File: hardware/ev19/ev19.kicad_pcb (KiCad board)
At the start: 4 copper layers, 173.8 x 91 mm, 254 parts, among them CN1 Conn_05x02_Female, CN3 BM14B(0.8)-24DS-0.4V(53), J1 USB_C_Receptacle, J10 USB_C_Receptacle, J11 Conn_02x05_Counter_Clockwise, J12 PJ-242, J2 Conn_01x02_Socket, J3 AudioJack4, J4 Conn_02x03_Odd_Even, J5 Conn_02x03_Odd_Even, J6 Conn_02x05_Counter_Clockwise, J7 Conn_02x05_Counter_Clockwise, J8 Conn_02x05_Counter_Clockwise, J9 Conn_02x05_Counter_Clockwise, Q1 2N7002, Q2 2N7002, Q3 2N7002, Q4 2N7002, Q5 2N7002, Q6 2N7002, SW1 SW_SPDT, SW2 SW_Push, SW3 SW_Push, SW4 SW_Push, SW5 SW_Push, SW6 SW_Push, SW7 SW_Push, U1 BQ21040DBV, U10 STM32F405RGTx, U12 XC6227C301MR-G, U2 USBLC6-2P6, U3 STM32F072CBTx, U4 CH340C, U5 TPS63060, U6 ES8311, U7 ESP32-S3-WROOM-1, U8 M24C02-RMN6TP, U9 TPS2116DRL, Y1 Crystal_GND24

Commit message: Change connector for display, but will need to change footprint
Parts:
- added J13: Conn_01x08_Pin, Connector_PinHeader_2.54mm:PinHeader_1x08_P2.54mm_Vertical_SMD_Pin1Left, F.Cu at (121.4, 56.1)
- added REF**: JST_PH_B2B-PH-SM4-TB_1x02-1MP_P2.00mm_Vertical, Connector_JST:JST_PH_B2B-PH-SM4-TB_1x02-1MP_P2.00mm_Vertical, F.Cu at (11.2, 131.4)
- added REF**: JST_PH_B8B-PH-SM4-TB_1x08-1MP_P2.00mm_Vertical, Connector_JST:JST_PH_B8B-PH-SM4-TB_1x08-1MP_P2.00mm_Vertical, F.Cu at (-13.2, 127.7)
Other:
- board text removed: "PTT buttons (screened)"

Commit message: Redesigned digital section again to fit the battery better. Chose where the screen connector and battery connector go
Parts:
- removed the H2 at (14.1, 73.3)
- removed J13: Conn_01x08_Pin, Connector_PinHeader_2.54mm:PinHeader_1x08_P2.54mm_Vertical_SMD_Pin1Left
- removed REF**: JST_PH_B2B-PH-SM4-TB_1x02-1MP_P2.00mm_Vertical, Connector_JST:JST_PH_B2B-PH-SM4-TB_1x02-1MP_P2.00mm_Vertical
- removed REF**: JST_PH_B8B-PH-SM4-TB_1x08-1MP_P2.00mm_Vertical, Connector_JST:JST_PH_B8B-PH-SM4-TB_1x08-1MP_P2.00mm_Vertical
- added H1: MountingHole, MountingHole:MountingHole_2.7mm_M2.5, F.Cu at (121.3, 112.9)
- added H2: MountingHole, MountingHole:MountingHole_2.7mm_M2.5, F.Cu at (140.8, 126.5)
- added H2: MountingHole, MountingHole:MountingHole_2.7mm_M2.5, F.Cu at (36.3, 112.8)
- added J14: Diplay_Connector, Connector_JST:JST_PH_S8B-PH-SM4-TB_1x08-1MP_P2.00mm_Horizontal, F.Cu at (100.3, 61.4)
- J2: value Conn_01x02_Socket -> BATT_CONN; footprint Hactar_Footprints:JST_PH_S2B-PH-SM4-TB_1x02-1MP_P2.00mm_Horizontal -> Connector_JST:JST_PH_S2B-PH-SM4-TB_1x02-1MP_P2.00mm_Horizontal
- SW4, SW5: footprint Hactar_Footprints:SW-SMD_4P-L5.1-W5.1-P3.70-LS6.5-TL_H1.5 -> Hactar_Footprints:SW-SMD_SHOU_TS36CA-0.6
- moved TP32 158.8 mm to (175.0, 63.5)
- moved J2 128.3 mm to (115.8, 61.4)
- moved TP31 117.1 mm to (121.7, 50.9)
- moved C12 116.4 mm to (120.8, 44.1), turned to 0 degrees
- moved R1 115.3 mm to (121.7, 32.6), turned to 180 degrees
- moved U1 115.0 mm to (120.2, 41.5), turned to 90 degrees
- moved JP1 114.4 mm to (121.7, 34.4)
- moved C4 113.7 mm to (119.7, 38.9), turned to 0 degrees
- moved R6 111.0 mm to (117.3, 42.0), turned to 90 degrees
- moved R65 110.4 mm to (118.2, 55.0), turned to 180 degrees
- moved D1 109.7 mm to (121.7, 48.5)
- moved R11 109.7 mm to (119.0, 48.5)
- moved TP26 100.5 mm to (111.0, 43.7)
- moved C39 100.5 mm to (76.8, 63.8)
- moved C40 100.5 mm to (65.2, 51.8)
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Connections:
- D2 pad 2: +3.3V -> GND
- D3 pad 2: +3.3V -> GND
- JP3 pad 3: +3.3V -> GND
- NT5 pad 1: +3.3V -> GND
- NT7 pad 1: +3.3V -> GND
- NT9 pad 1: +3.3V -> GND
- SW4 pad 2: +3.3V -> Net-(C46-Pad1)
- SW5 pad 2: +3.3V -> Net-(C47-Pad1)
- SW6 pad 1: +3.3V -> GND
- SW7 pad 1: +3.3V -> GND
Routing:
- net Net-(J2-Pin_2): track 32.6 -> 10.4 mm, vias 6 -> 3
- net GND: track 38.6 -> 54.4 mm, vias 48 -> 64
- net +3.3V: track 14.3 -> 1.80 mm, vias 25 -> 10
- net VSYS: track 11.7 -> 0.00 mm, vias 6 -> 0
- net Net-(D2-RK): track 5.50 -> 15.1 mm
- net Net-(D3-GK): track 6.30 -> 14.4 mm
- net Net-(Q6-G): track 9.94 -> 1.86 mm
- net Net-(D3-RK): track 5.96 -> 13.8 mm
- net Net-(D2-GK): track 5.77 -> 13.5 mm
- net Net-(D1-K): track 15.0 -> 8.54 mm
- net Net-(JP3-C): track 6.22 -> 0.00 mm
- net /BQ_OUT: track 14.0 -> 18.6 mm, vias 4 -> 6
- net Net-(JP1-B): track 5.11 -> 2.05 mm
- net Net-(JP1-C): track 10.1 -> 7.10 mm
- net Net-(C63-Pad1): track 10.7 -> 8.37 mm
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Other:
- board size 173.8 x 91 mm -> 71.5 x 91 mm
- board text added: "30.5mm 44.0mm"
- board text removed: "+3.3V"
- board text removed: "BATTERY"
- board text removed: "BOARD"
- board text removed: "BOOT0"
- board text removed: "DEV"
- board text removed: "ESP-PROG"
- board text removed: "GND"
- board text removed: "I2S_ADCDAT"
- board text removed: "I2S_BCLK"
- board text removed: "I2S_DACDAT"
- board text removed: "I2S_DACLRC"
- board text removed: "MCLK"
- board text removed: "MGMT STLINK"
- board text removed: "MGMT_DEBUG_1"
- board text removed: "MGMT_DEBUG_2"
- board text removed: "NET_BOOT"
- board text removed: "NET_DEBUG_1"
- board text removed: "NET_DEBUG_2"
- board text removed: "NET_DEBUG_3"
- board text removed: "NET_NRST"
- board text removed: "NET_RX1_MGMT"
- board text removed: "NET_TX1_MGMT"
- board text removed: "NRST"
- board text removed: "SPI1_CLK"
- board text removed: "SPI1_MISO"
- board text removed: "SPI1_MOSI"
- board text removed: "SWCLK"
- board text removed: "SWDIO"
- board text removed: "UI STLINK"
- board text removed: "UI_CTS1_MGMT"
- board text removed: "UI_DEBUG_1"
- board text removed: "UI_DEBUG_2"
- board text removed: "UI_RTS1_MGMT"
- board text removed: "UI_RX1_MGMT"
- board text removed: "UI_RX2_NET"
- board text removed: "UI_SCL"
- board text removed: "UI_SDA"
- board text removed: "UI_TX1_MGMT"
- board text removed: "UI_TX2_NET"
- board text removed: "USB_RX1_MGMT"
- board text removed: "USB_TX1_MGMT"
- board text removed: "X"

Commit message: Changed debug ports to 32pin female headers, laid out more of the digital section, drew square where screen should sit
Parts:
- removed CN1: Conn_05x02_Female, Hactar_Footprints:IDC-SMD_10P-P1.27_X1270WVS-2X05B-6TV01
- removed the H4 at (144.9, 71.5)
- removed the H5 at (88.5, 98.6)
- removed J10: USB_C_Receptacle, Connector_USB:USB_C_Receptacle_HRO_TYPE-C-31-M-12
- removed J11, J6, J7, J8, J9: Conn_02x05_Counter_Clockwise, Hactar_Footprints:HDR-SMD_10P-P2.54-V-F-R2-C5-LS7.1-1
- removed J4, J5: Conn_02x03_Odd_Even, Hactar_Footprints:HDR-SMD_6P-P2.54-V-M-R2-C3-LS7.5-2
- removed R72: 1k0, Resistor_SMD:R_0402_1005Metric
- moved Q1 110.5 mm to (61.6, 63.6), turned to 0 degrees
- moved SW2 98.9 mm to (54.7, 70.4)
- moved SW3 96.6 mm to (54.7, 75.9), turned to 90 degrees
- moved R88 80.8 mm to (74.1, 85.2), turned to 0 degrees
- moved H5 59.3 mm to (88.5, 98.6)
- moved NT6 36.5 mm to (75.5, 77.5), turned to 180 degrees
- moved R77 31.1 mm to (72.6, 77.5), turned to 180 degrees
- moved R50 31.0 mm to (75.5, 86.2)
- moved Q5 23.2 mm to (19.1, 66.1)
- moved Q2 23.1 mm to (19.1, 70.2)
- moved Q4 21.0 mm to (115.3, 39.9)
- moved R12 20.7 mm to (19.2, 62.1)
- moved R61 20.4 mm to (74.4, 80.5), turned to -90 degrees
- moved R5 20.4 mm to (58.9, 81.2), turned to -90 degrees
- moved R34 20.4 mm to (118.3, 30.6), turned to 180 degrees
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- renumbered H3 to H1, H1 to H2, H2 to H3, H1 to H4, H2 to H5
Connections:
- net /USB_DTR renamed /USB_DTR_MGMT
- net /USB_RTS renamed /USB_RTS_MGMT
- D2 pad 2: GND -> +3.3V
- D3 pad 2: GND -> +3.3V
- JP3 pad 3: GND -> +3.3V
- NT5 pad 1: GND -> +3.3V
- NT7 pad 1: GND -> +3.3V
- NT9 pad 1: GND -> +3.3V
- R66 pad 1: /I2S_ADCDAT -> /I2S_DACLRC
- R67 pad 1: /I2S_DACLRC -> /I2S_DACDAT
- R68 pad 1: /I2S_DACDAT -> /I2S_BCLK
- R69 pad 1: /I2S_BCLK -> /I2S_ADCDAT
- SW6 pad 1: GND -> +3.3V
- SW7 pad 1: GND -> +3.3V
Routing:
- net VBUS: track 6.39 -> 53.6 mm
- net Net-(SW1-A): track 5.21 -> 44.2 mm, vias 4 -> 5
- net Net-(J2-Pin_2): track 10.4 -> 39.9 mm, vias 3 -> 4
- net /MGMT_LED_B: track 0.00 -> 17.0 mm, vias 0 -> 2
- net GND: track 54.4 -> 68.4 mm, vias 64 -> 59
- net Net-(D2-GK): track 13.5 -> 0.00 mm
- net +3.3V: track 1.80 -> 15.2 mm, vias 10 -> 24
- net /MGMT_LED_R: track 0.00 -> 13.2 mm
- net Net-(D2-RK): track 15.1 -> 2.12 mm
- net Net-(Q1-D): track 0.00 -> 12.7 mm, vias 0 -> 2
- net Net-(Q4-D): track 0.00 -> 11.6 mm
- net Net-(D3-GK): track 14.4 -> 3.17 mm
- net Net-(D3-RK): track 13.8 -> 2.66 mm
- net /RCC_OSC_IN: track 0.00 -> 10.8 mm
- net Net-(JP3-C): track 0.00 -> 9.12 mm
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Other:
- outline, holes or cut-outs redrawn
- board text added: "JST connector 20mm"
- board text added: "JST to Edge 17mm"
- board text added: "TODO fit a hole somewhere to give the center piece more support"
- board text removed: "Mount"

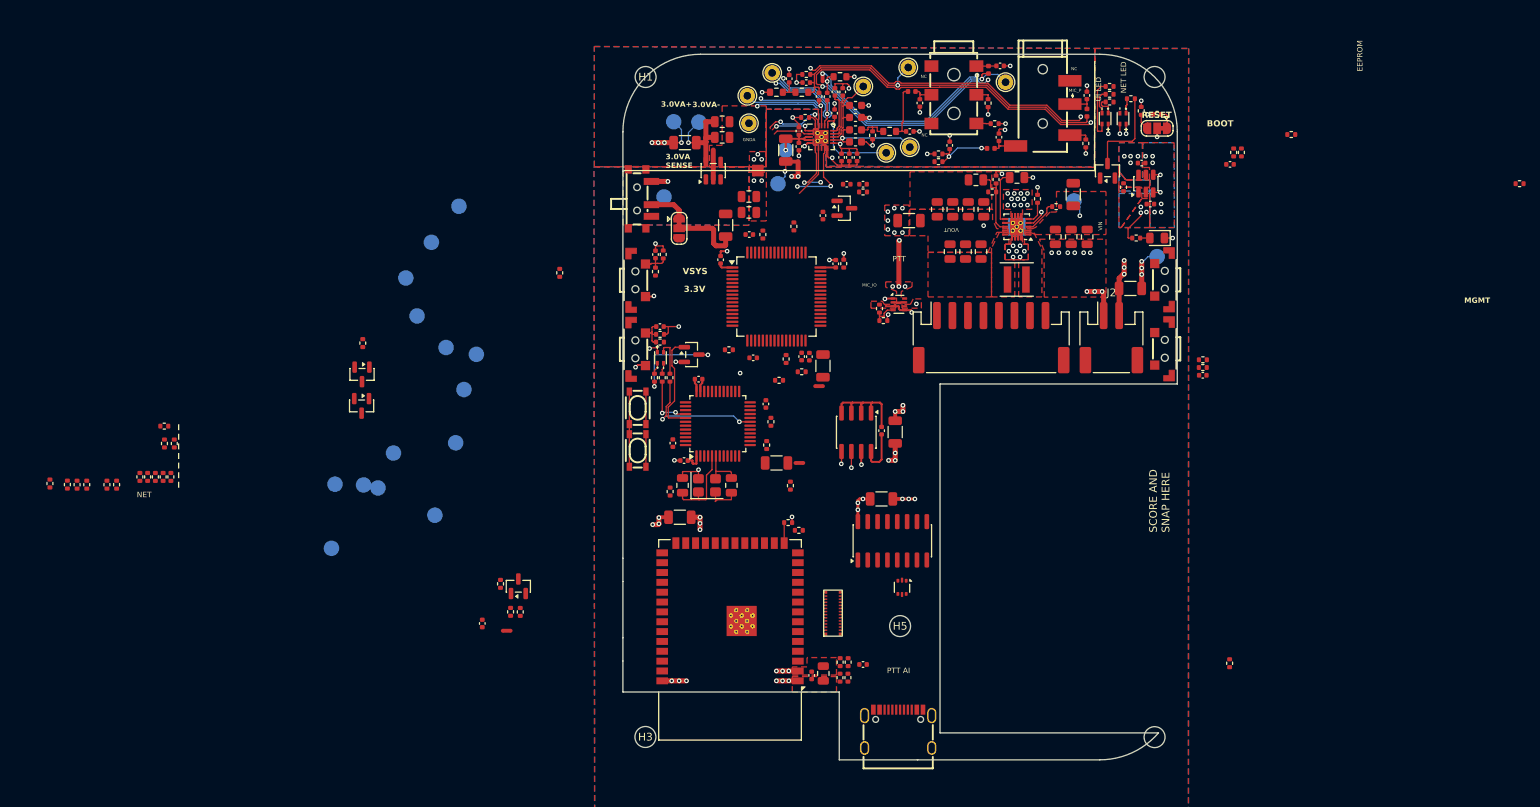
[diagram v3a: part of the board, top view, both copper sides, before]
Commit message: Fit in a debug connector to go to a dev board
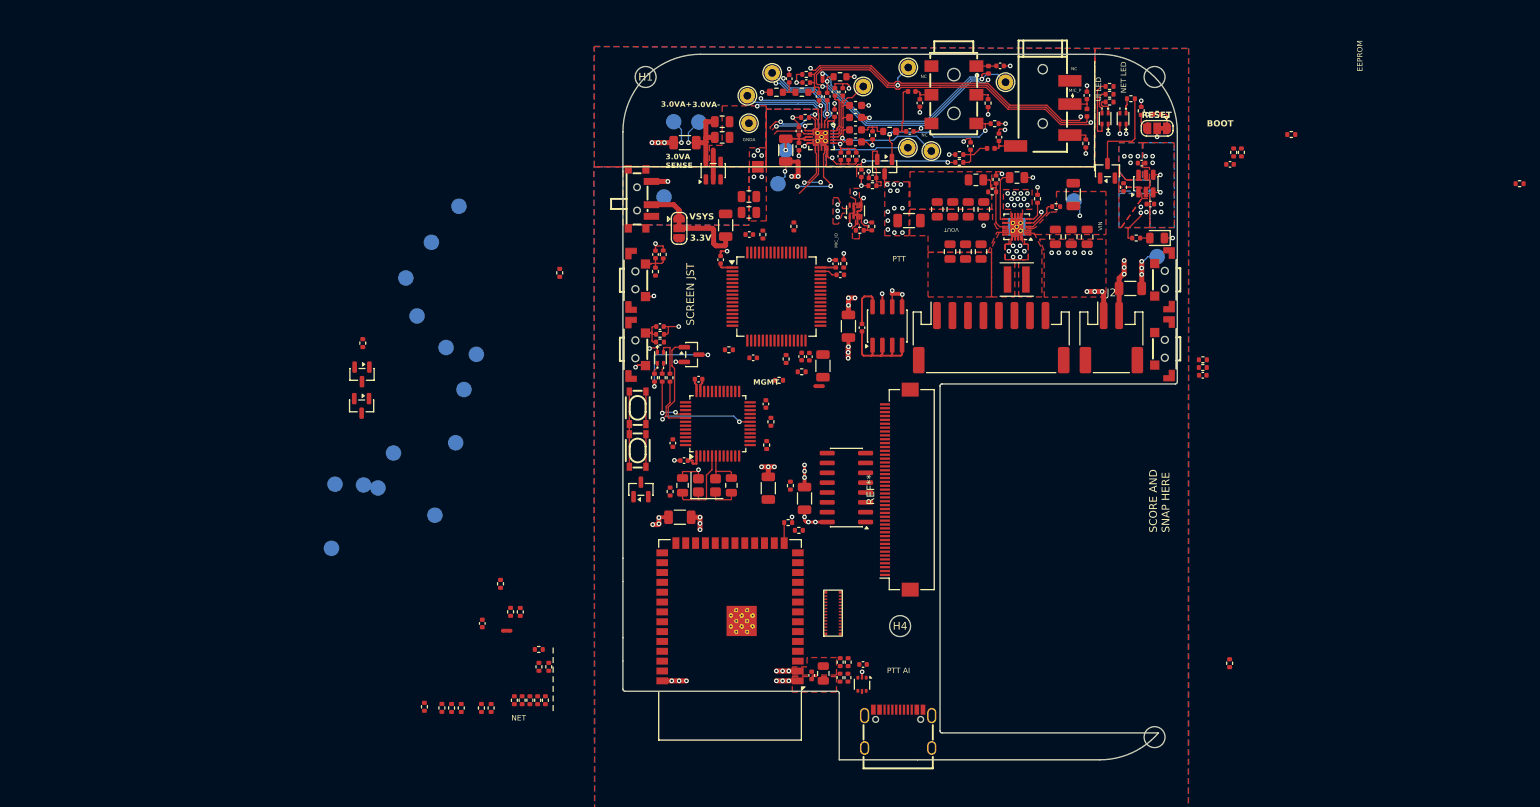
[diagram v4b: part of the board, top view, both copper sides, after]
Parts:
- removed the H3 at (55.7, 112.9)
- added REF**: Hirose_FH12-45S-0.5SH_1x45-1MP_P0.50mm_Horizontal, Connector_FFC-FPC:Hirose_FH12-45S-0.5SH_1x45-1MP_P0.50mm_Horizontal, F.Cu at (88.4, 81.0)
- moved R70 56.2 mm to (43.2, 103.8)
- moved R73 56.2 mm to (41.9, 101.6)
- moved R30 56.2 mm to (35.8, 109.1)
- moved R4 56.2 mm to (27.2, 109.0)
- moved R44 56.2 mm to (30.7, 109.1)
- moved R45 56.2 mm to (29.4, 109.1)
- moved R46 56.2 mm to (31.9, 109.1)
- moved R49 56.2 mm to (34.5, 109.1)
- moved R64 56.2 mm to (42.8, 108.1)
- moved R66 56.2 mm to (41.8, 108.1)
- moved R67 56.2 mm to (39.8, 108.1)
- moved R68 56.2 mm to (40.8, 108.1)
- moved R69 56.2 mm to (38.8, 108.1)
- moved R71 56.2 mm to (41.9, 103.8)
- moved NT6 25.1 mm to (87.9, 55.7), turned to 0 degrees
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- renumbered H4 to H3, H5 to H4
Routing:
- net VBUS: track 53.6 -> 26.3 mm
- net Net-(Q6-G): track 1.86 -> 19.2 mm, vias 0 -> 2
- net Net-(SW1-A): track 44.2 -> 28.3 mm, vias 5 -> 4
- net /Audio/MIC_PTT_BTN: track 0.00 -> 15.2 mm, vias 0 -> 2
- net Net-(J2-Pin_2): track 39.9 -> 53.9 mm
- net /Audio/nJACK_R1N: track 0.00 -> 7.51 mm
- net GND: track 68.4 -> 71.6 mm, vias 59 -> 61
- net /Audio/OUTP: track 14.0 -> 17.1 mm
- net +3.3V_Mgmt: track 4.13 -> 7.08 mm, vias 0 -> 3
- net /Audio/AMID: track 12.4 -> 15.1 mm
- net Net-(C63-Pad1): track 8.37 -> 5.85 mm, vias 2 -> 0
- net Net-(U10-VCAP_2): track 0.00 -> 2.40 mm
- net +3.3V: track 15.2 -> 16.6 mm, vias 24 -> 29
- net GNDA: track 195.1 -> 195.8 mm
- net +3.0VA: track 16.2 -> 15.5 mm
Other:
- outline, holes or cut-outs redrawn
- board text added: "SCREEN JST"
